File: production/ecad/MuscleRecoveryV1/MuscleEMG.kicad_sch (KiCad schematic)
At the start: 38 parts, among them J1 AudioJack3, J2 Screw_Terminal_01x03, J5 Screw_Terminal_01x04, U5 AD8232ACPZ-R7, U7 ADS1115IDGS

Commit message: Footprints added
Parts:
- D5, D6: footprint (none) -> LED_THT:LED_D1.8mm_W3.3mm_H2.4mm
- R24, R46, R47, R48, R49: footprint (none) -> Resistor_SMD:R_0805_2012Metric
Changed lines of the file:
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@@
       (effects (font (size 1.27 1.27)))
     )
-    (property "Footprint" "" (at 66.04 173.228 90)
+    (property "Footprint" "Resistor_SMD:R_0805_2012Metric" (at 66.04 173.228 90)
       (effects (font (size 1.27 1.27)) hide)
     )
@@
       (effects (font (size 1.27 1.27)))
     )
-    (property "Footprint" "" (at 238.76 77.47 0)
+    (property "Footprint" "LED_THT:LED_D1.8mm_W3.3mm_H2.4mm" (at 238.76 77.47 0)
       (effects (font (size 1.27 1.27)) hide)
     )
@@
       (effects (font (size 1.27 1.27)))
     )
-    (property "Footprint" "" (at 165.1 107.188 90)
+    (property "Footprint" "Resistor_SMD:R_0805_2012Metric" (at 165.1 107.188 90)
       (effects (font (size 1.27 1.27)) hide)
     )
@@
       (effects (font (size 1.27 1.27)))
     )
-    (property "Footprint" "" (at 154.94 105.41 0)
+    (property "Footprint" "LED_THT:LED_D1.8mm_W3.3mm_H2.4mm" (at 154.94 105.41 0)
       (effects (font (size 1.27 1.27)) hide)
     )
@@
       (effects (font (size 1.27 1.27)))
     )
-    (property "Footprint" "" (at 66.04 175.768 90)
+    (property "Footprint" "Resistor_SMD:R_0805_2012Metric" (at 66.04 175.768 90)
       (effects (font (size 1.27 1.27)) hide)
     )
@@
       (effects (font (size 1.27 1.27)))
     )
-    (property "Footprint" "" (at 144.78 107.188 90)
+    (property "Footprint" "Resistor_SMD:R_0805_2012Metric" (at 144.78 107.188 90)
       (effects (font (size 1.27 1.27)) hide)
     )
@@
       (effects (font (size 1.27 1.27)))
     )
-    (property "Footprint" "" (at 62.23 168.148 90)
-      (effects (font (size 1.27 1.27)) hide)
-    )
+    (property "Footprint" "Resistor_SMD:R_0805_2012Metric" (at 62.23 168.148 90)
+      (effects (font (size 1.27 1.27)) hide)
+    )

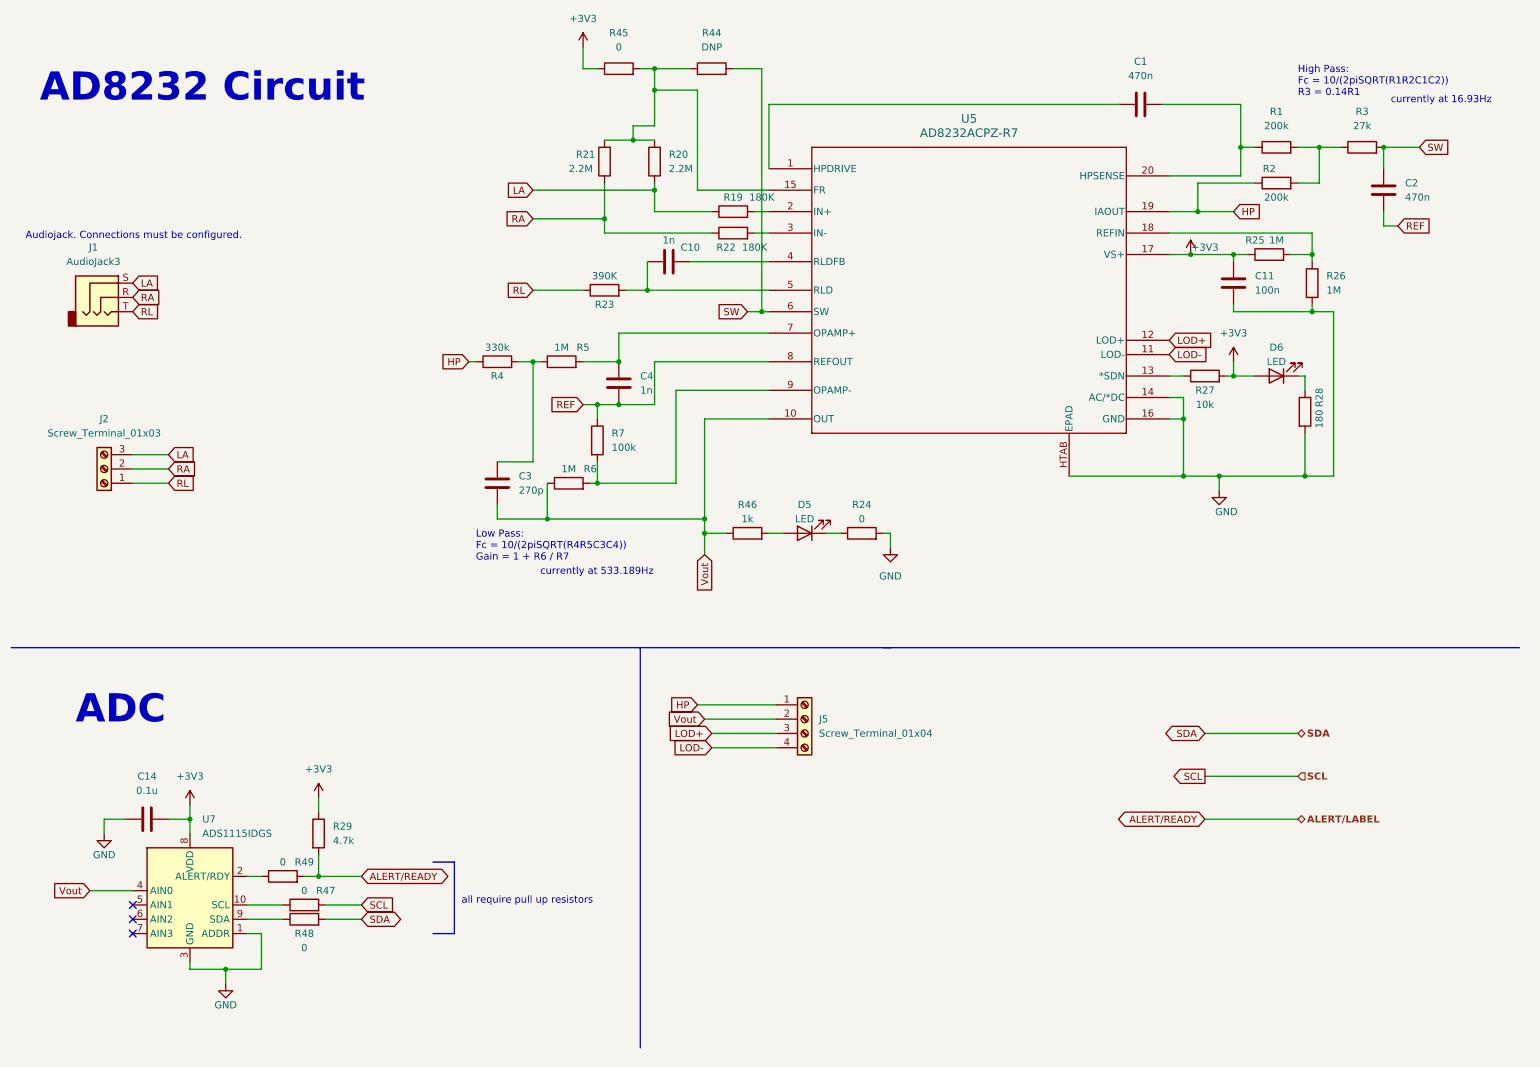
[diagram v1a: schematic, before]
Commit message: updates to emg schematic from Alex and Sean suggestions
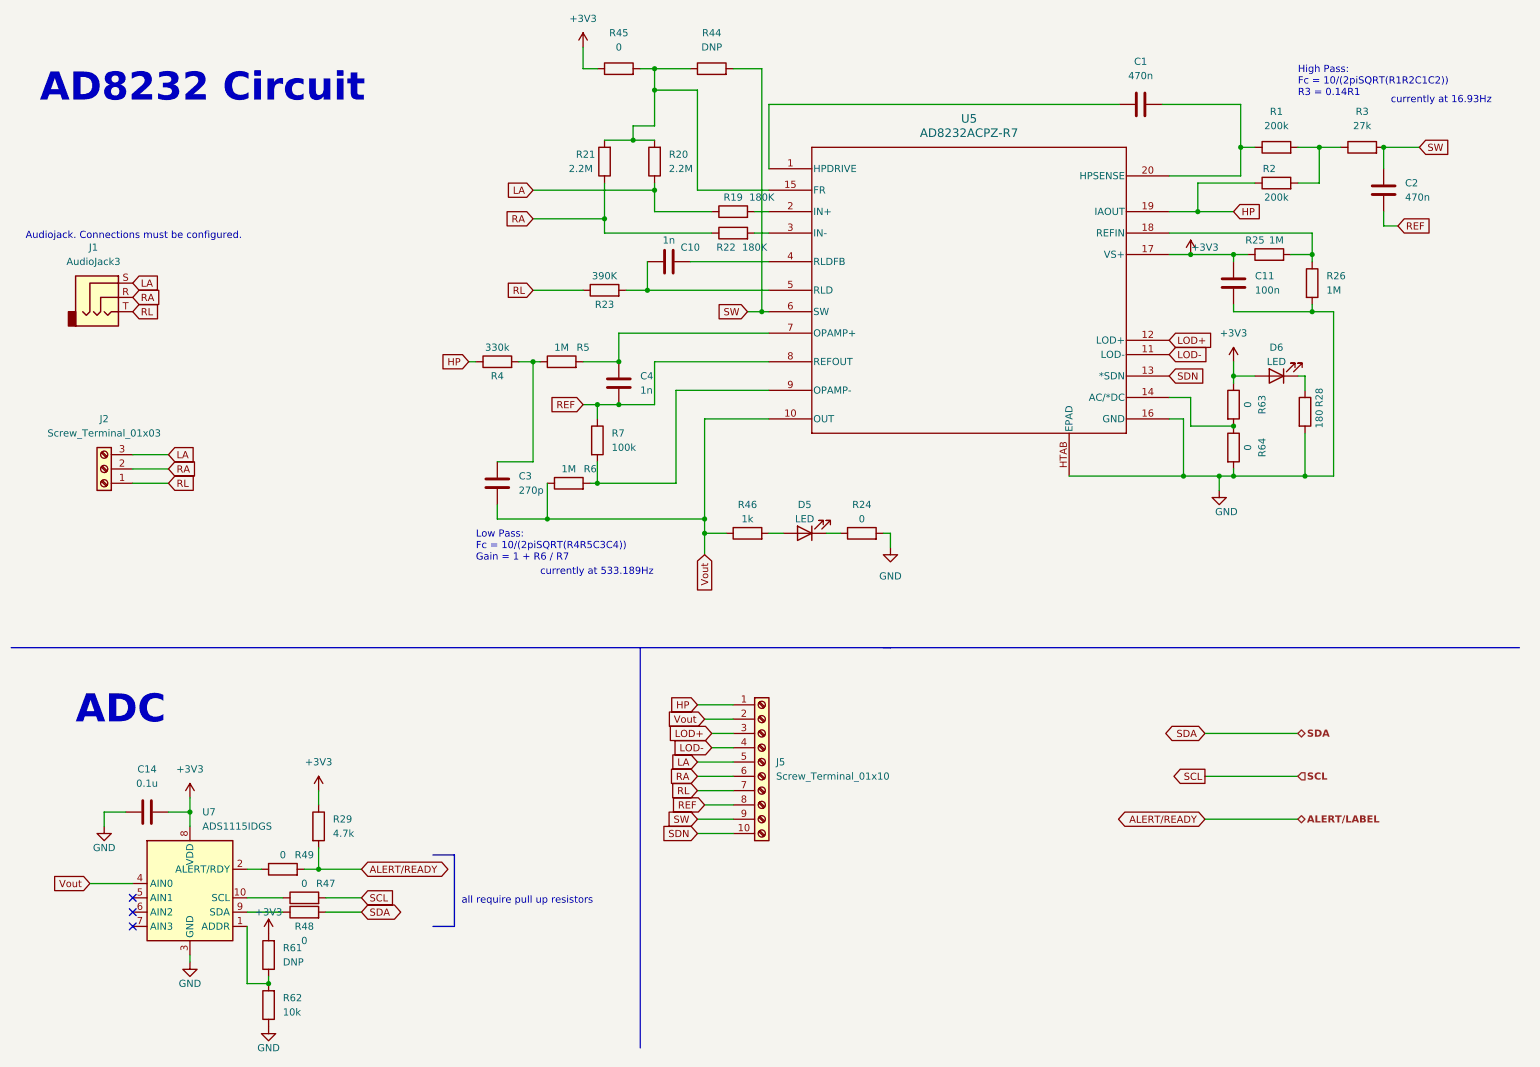
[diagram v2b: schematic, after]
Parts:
- removed J5: Screw_Terminal_01x04, symbol Connector:Screw_Terminal_01x04
- removed R27: 10k, Resistor_SMD:R_0805_2012Metric, symbol Device:R
- added J5: Screw_Terminal_01x10, symbol Connector:Screw_Terminal_01x10
- added R61: DNP, Resistor_SMD:R_0805_2012Metric, symbol Device:R
- added R62: 10k, Resistor_SMD:R_0805_2012Metric, symbol Device:R
- added R63, R64: 0, Resistor_SMD:R_0805_2012Metric, symbol Device:R
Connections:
- net +3V3: now also R61.2, R63.1
- net GND: now also R62.1, R64.2; no longer U5.14 (AC/*DC), U7.1 (ADDR)
- net HP: now also J5.1 (Pin_1)
- net LA: now also J5.5 (Pin_5)
- net LOD+: now also J5.3 (Pin_3)
- net LOD-: now also J5.4 (Pin_4)
- net RA: now also J5.6 (Pin_6)
- net REF: now also J5.8 (Pin_8)
- net RL: now also J5.7 (Pin_7)
- net SW: now also J5.9 (Pin_9)
- net Vout: now also J5.2 (Pin_2)
- net SDN: now reaches U5.13 (*SDN)
- net SDN: now also J5.10 (Pin_10)
- new net: R63.2, R64.1, U5.14 (AC/*DC)
- new net: R61.1, R62.2, U7.1 (ADDR)
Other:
- moved on the sheet: C14, R29, R47, R48, R49, U7

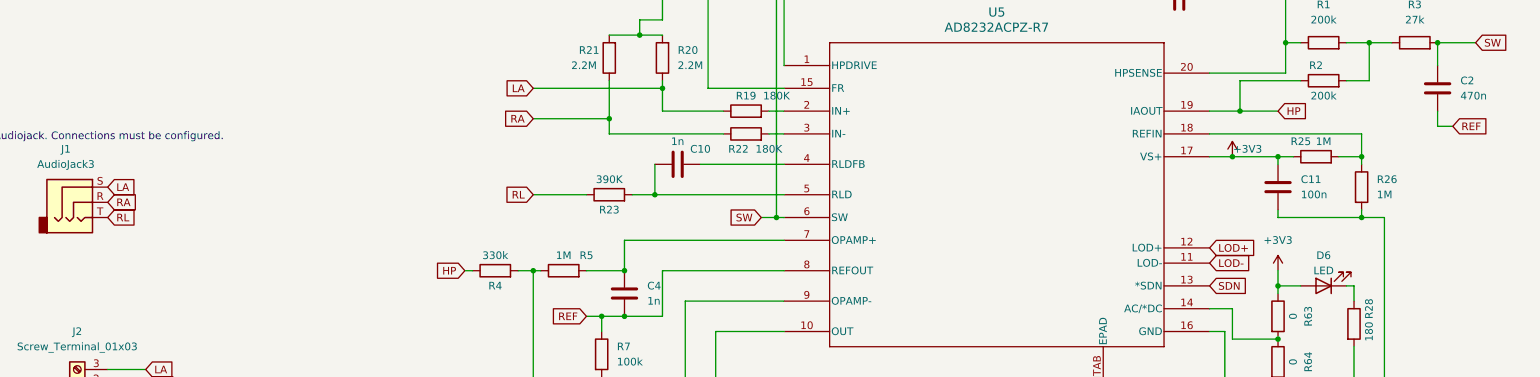
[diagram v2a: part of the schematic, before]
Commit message: updated footprints and emg schematic
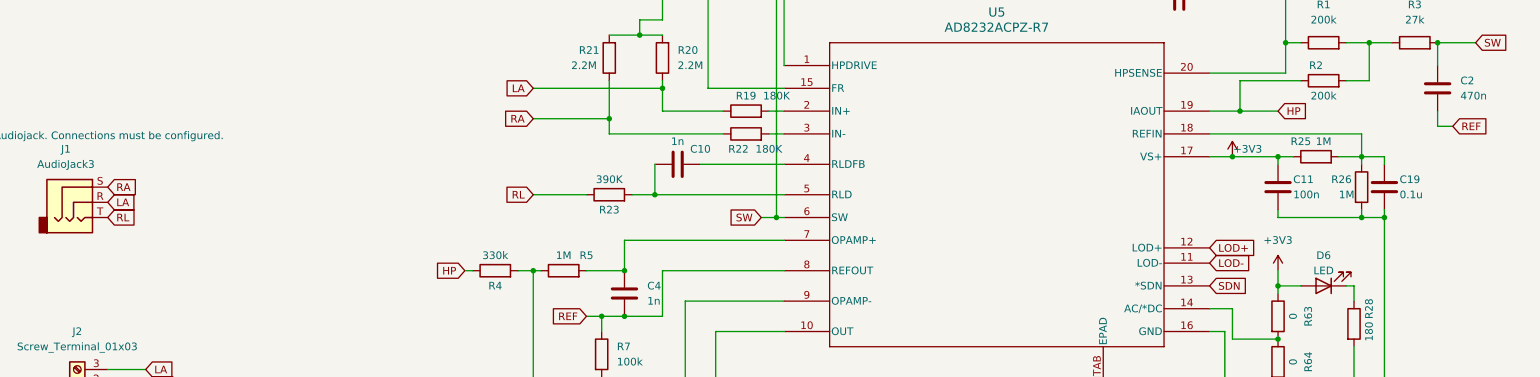
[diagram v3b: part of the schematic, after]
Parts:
- added C19: 0.1u, Capacitor_SMD:C_0805_2012Metric, symbol Device:C
- J1: footprint (none) -> Muscle_Recovery_Footprint_Library:CUI_SJ-3523-SMT-TR
- J2: footprint (none) -> Connector_PinHeader_2.54mm:PinHeader_1x03_P2.54mm_Horizontal
- J5: footprint (none) -> Connector_PinHeader_2.54mm:PinHeader_1x10_P2.54mm_Horizontal
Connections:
- net GND: now also C19.2
- net LA: now also J1.R; no longer J1.S
- net RA: now also J1.S; no longer J1.R
- net at R25.2, R26.1, U5.18 (REFIN): now also C19.1
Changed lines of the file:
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@@
   (junction (at 228.6 95.25) (diameter 0) (color 0 0 0 0)
+  )
+  (junction (at 248.92 66.04) (diameter 0) (color 0 0 0 0)
   )
   (junction (at 121.92 74.93) (diameter 0) (color 0 0 0 0)
@@
     (stroke (width 0) (type default))
   )
+  (wire (pts (xy 248.92 64.77) (xy 248.92 66.04))
+    (stroke (width 0) (type default))
+  )
   (wire (pts (xy 45.72 181.61) (xy 45.72 180.34))
     (stroke (width 0) (type default))
@@
     (stroke (width 0) (type default))
   )
+  (wire (pts (xy 248.92 57.15) (xy 248.92 55.88))
+    (stroke (width 0) (type default))
+  )
   (wire (pts (xy 231.14 74.93) (xy 231.14 77.47))
     (stroke (width 0) (type default))
@@
   )
   (wire (pts (xy 144.78 66.04) (xy 147.32 66.04))
+    (stroke (width 0) (type default))
+  )
+  (wire (pts (xy 248.92 55.88) (xy 245.11 55.88))
     (stroke (width 0) (type default))
   )
@@
     (effects (font (size 5 5) bold) (justify left bottom))
   )
-  (global_label "RA" (shape input) (at 35.56 63.5 0) (fields_autoplaced)
+  (global_label "RA" (shape input) (at 35.56 60.96 0) (fields_autoplaced)
     (effects (font (size 1.27 1.27)) (justify left))
-    (property "Intersheetrefs" "${INTERSHEET_REFS}" (at 40.9038 63.5 0)
+    (property "Intersheetrefs" "${INTERSHEET_REFS}" (at 40.9038 60.96 0)
       (effects (font (size 1.27 1.27)) (justify left) hide)
     )
@@
     )
   )
-  (global_label "LA" (shape input) (at 35.56 60.96 0) (fields_autoplaced)
+  (global_label "LA" (shape input) (at 35.56 63.5 0) (fields_autoplaced)
     (effects (font (size 1.27 1.27)) (justify left))
-    (property "Intersheetrefs" "${INTERSHEET_REFS}" (at 40.6619 60.96 0)
+    (property "Intersheetrefs" "${INTERSHEET_REFS}" (at 40.6619 63.5 0)
       (effects (font (size 1.27 1.27)) (justify left) hide)
     )
@@
       (effects (font (size 1.27 1.27)))
     )
-    (property "Footprint" "" (at 30.48 93.98 0)
+    (property "Footprint" "Connector_PinHeader_2.54mm:PinHeader_1x03_P2.54mm_Horizontal" (at 30.48 93.98 0)
       (effects (font (size 1.27 1.27)) hide)
     )
@@
   )
   (symbol (lib_id "Device:R") (at 245.11 60.96 0) (unit 1)
-    (in_bom yes) (on_board yes) (dnp no) (fields_autoplaced)
-    (property "Reference" "R26" (at 247.65 59.69 0)
+    (in_bom yes) (on_board yes) (dnp no)
+    (property "Reference" "R26" (at 240.03 59.69 0)
       (effects (font (size 1.27 1.27)) (justify left))
     )
-    (property "Value" "1M" (at 247.65 62.23 0)
+    (property "Value" "1M" (at 241.3 62.23 0)
       (effects (font (size 1.27 1.27)) (justify left))
     )
@@
       (effects (font (size 1.27 1.27)) (justify left))
     )
-    (property "Footprint" "" (at 147.32 146.05 0)
+    (property "Footprint" "Connector_PinHeader_2.54mm:PinHeader_1x10_P2.54mm_Horizontal" (at 147.32 146.05 0)
       (effects (font (size 1.27 1.27)) hide)
     )
@@
     )
   )
+  (symbol (lib_id "Device:C") (at 248.92 60.96 0) (unit 1)
+    (in_bom yes) (on_board yes) (dnp no)
+    (property "Reference" "C19" (at 251.46 59.69 0)
+      (effects (font (size 1.27 1.27)) (justify left))
+    )
+    (property "Value" "0.1u" (at 251.46 62.23 0)
+      (effects (font (size 1.27 1.27)) (justify left))
+    )
+    (property "Footprint" "Capacitor_SMD:C_0805_2012Metric" (at 249.8852 64.77 0)
+      (effects (font (size 1.27 1.27)) hide)
+    )
+    (property "Datasheet" "~" (at 248.92 60.96 0)
+      (effects (font (size 1.27 1.27)) hide)
+    )
+    (pin "1")
+    (pin "2")
+    (instances
+      (project "MuscleRecoveryV1"
+        (path "/4e550305-79d2-4e4a-a502-817ebcc79f9a/284c60dd-e199-4b03-b99f-cc7eaed256f8"
+          (reference "C19") (unit 1)
+        )
+      )
+    )
+  )
   (symbol (lib_id "Device:R") (at 165.1 105.41 90) (unit 1)
     (in_bom yes) (on_board yes) (dnp no)
@@
       (effects (font (size 1.27 1.27)))
     )
-    (property "Footprint" "" (at 30.48 63.5 0)
+    (property "Footprint" "Muscle_Recovery_Footprint_Library:CUI_SJ-3523-SMT-TR" (at 30.48 63.5 0)
       (effects (font (size 1.27 1.27)) hide)
     )
@@
   )
   (symbol (lib_id "Device:C") (at 231.14 60.96 0) (unit 1)
-    (in_bom yes) (on_board yes) (dnp no) (fields_autoplaced)
-    (property "Reference" "C11" (at 234.95 59.69 0)
+    (in_bom yes) (on_board yes) (dnp no)
+    (property "Reference" "C11" (at 233.68 59.69 0)
       (effects (font (size 1.27 1.27)) (justify left))
     )
-    (property "Value" "100n" (at 234.95 62.23 0)
+    (property "Value" "100n" (at 233.68 62.23 0)
       (effects (font (size 1.27 1.27)) (justify left))
     )

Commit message: supposedly finished schematic and footprints and started PCB
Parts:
- J2: footprint Connector_PinHeader_2.54mm:PinHeader_1x03_P2.54mm_Horizontal -> Connector_PinHeader_2.54mm:PinHeader_1x03_P2.54mm_Vertical
- J5: footprint Connector_PinHeader_2.54mm:PinHeader_1x10_P2.54mm_Horizontal -> Connector_PinHeader_2.54mm:PinHeader_1x10_P2.54mm_Vertical
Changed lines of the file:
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@@
       (effects (font (size 1.27 1.27)))
     )
-    (property "Footprint" "Connector_PinHeader_2.54mm:PinHeader_1x03_P2.54mm_Horizontal" (at 30.48 93.98 0)
+    (property "Footprint" "Connector_PinHeader_2.54mm:PinHeader_1x03_P2.54mm_Vertical" (at 30.48 93.98 0)
       (effects (font (size 1.27 1.27)) hide)
     )
@@
       (effects (font (size 1.27 1.27)) (justify left))
     )
-    (property "Footprint" "Connector_PinHeader_2.54mm:PinHeader_1x10_P2.54mm_Horizontal" (at 147.32 146.05 0)
-      (effects (font (size 1.27 1.27)) hide)
-    )
+    (property "Footprint" "Connector_PinHeader_2.54mm:PinHeader_1x10_P2.54mm_Vertical" (at 147.32 146.05 0)
+      (effects (font (size 1.27 1.27)) hide)
+    )

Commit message: pushing current layout and other changes to be able to pull
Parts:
- removed J5: Screw_Terminal_01x10, Connector_PinHeader_2.54mm:PinHeader_1x10_P2.54mm_Vertical, symbol Connector:Screw_Terminal_01x10
- added J8: Screw_Terminal_01x07, Connector_PinHeader_2.54mm:PinHeader_1x07_P2.54mm_Vertical, symbol Connector:Screw_Terminal_01x07
- R63: value 0 -> DNP
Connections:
- net HP: now also J8.1 (Pin_1)
- net LA: now also J1.3; no longer J1.R
- net LOD+: now also J8.3 (Pin_3)
- net LOD-: now also J8.4 (Pin_4)
- net RA: now also J1.1; no longer J1.S
- net REF: now also J8.5 (Pin_5)
- net RL: now also J1.2; no longer J1.T
- net SDN: now also J8.7 (Pin_7)
- net SW: now also J8.6 (Pin_6)
- net Vout: now also J8.2 (Pin_2)
